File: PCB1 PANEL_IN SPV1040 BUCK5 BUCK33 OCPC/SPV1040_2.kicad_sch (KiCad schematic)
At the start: 14 parts, among them J3 SOLAR, U3 SPV1040TTR

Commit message: w
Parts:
- removed D4: D_Zener, Diode_SMD:D_1210_3225Metric, symbol Device:D_Zener
- added CR3: SMM4F5.0A-TR, CR_F5.0A-TR_STM, symbol SMM4F5:SMM4F5.0A-TR
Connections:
- net GND: now also CR3.1
- net PANEL1_OUT: now also CR3.2
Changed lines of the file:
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@@
-	(wire
-		(pts
-			(xy 104.14 102.87) (xy 106.68 102.87)
-		)
-		(stroke
-			(width 0)
-			(type default)
-		)
-	)
 	(wire
 		(pts
@@
 	)
 	(symbol
+		(lib_id "SMM4F5:SMM4F5.0A-TR")
+		(at 96.52 102.87 0)
+		(unit 1)
+		(exclude_from_sim no)
+		(in_bom yes)
+		(on_board yes)
+		(dnp no)
+		(fields_autoplaced yes)
+		(property "Reference" "CR3"
+			(at 101.6 96.52 0)
+			(effects
+				(font
+					(size 1.524 1.524)
+				)
+			)
+		)
+		(property "Value" "SMM4F5.0A-TR"
+			(at 101.6 99.06 0)
+			(effects
+				(font
+					(size 1.524 1.524)
+				)
+			)
+		)
+		(property "Footprint" "CR_F5.0A-TR_STM"
+			(at 96.52 102.87 0)
+			(effects
+				(font
+					(size 1.27 1.27)
+					(italic yes)
+				)
+				(hide yes)
+			)
+		)
+		(property "Datasheet" "SMM4F5.0A-TR"
+			(at 96.52 102.87 0)
+			(effects
+				(font
+					(size 1.27 1.27)
+					(italic yes)
+				)
+				(hide yes)
+			)
+		)
+		(property "Description" ""
+			(at 96.52 102.87 0)
+			(effects
+				(font
+					(size 1.27 1.27)
+				)
+				(hide yes)
+			)
+		)
+		(pin "1"
+		)
+		(pin "2"
+		)
+		(instances
+			(project "PCB1 PANEL_IN SPV1040 BUCK5 BUCK33 OCPC"
+				(path "/494c9d9f-6b33-4248-a813-27ffaaa929bd/27d3faa1-92c4-4207-bb91-69c494af1bc4"
+					(reference "CR3")
+					(unit 1)
+				)
+			)
+		)
+	)
+	(symbol
 		(lib_id "Device:R")
 		(at 124.46 52.07 0)
@@
 					(unit 1)
 				)
-			)
-		)
-	)
-	(symbol
-		(lib_id "Device:D_Zener")
-		(at 100.33 102.87 180)
-		(unit 1)
-		(exclude_from_sim no)
-		(in_bom yes)
-		(on_board yes)
-		(dnp no)
-		(fields_autoplaced yes)
-		(property "Reference" "D4"
-			(at 100.33 96.52 0)
-			(effects
-				(font
-					(size 1.27 1.27)
-				)
-			)
-		)
-		(property "Value" "D_Zener"
-			(at 100.33 99.06 0)
-			(effects
-				(font
-					(size 1.27 1.27)
-				)
-			)
-		)
-		(property "Footprint" "Diode_SMD:D_1210_3225Metric"
-			(at 100.33 102.87 0)
-			(effects
-				(font
-					(size 1.27 1.27)
-				)
-				(hide yes)
-			)
-		)
-		(property "Datasheet" "~"
-			(at 100.33 102.87 0)
-			(effects
-				(font
-					(size 1.27 1.27)
-				)
-				(hide yes)
-			)
-		)
-		(property "Description" "Zener diode"
-			(at 100.33 102.87 0)
-			(effects
-				(font
-					(size 1.27 1.27)
-				)
-				(hide yes)
-			)
-		)
-		(pin "2"
-		)
-		(pin "1"
-		)
-		(instances
-			(project "PCB1 PANEL_IN SPV1040 BUCK5 BUCK33 OCPC"
-				(path "/494c9d9f-6b33-4248-a813-27ffaaa929bd/27d3faa1-92c4-4207-bb91-69c494af1bc4"
-					(reference "D4")
-					(unit 1)
-				)

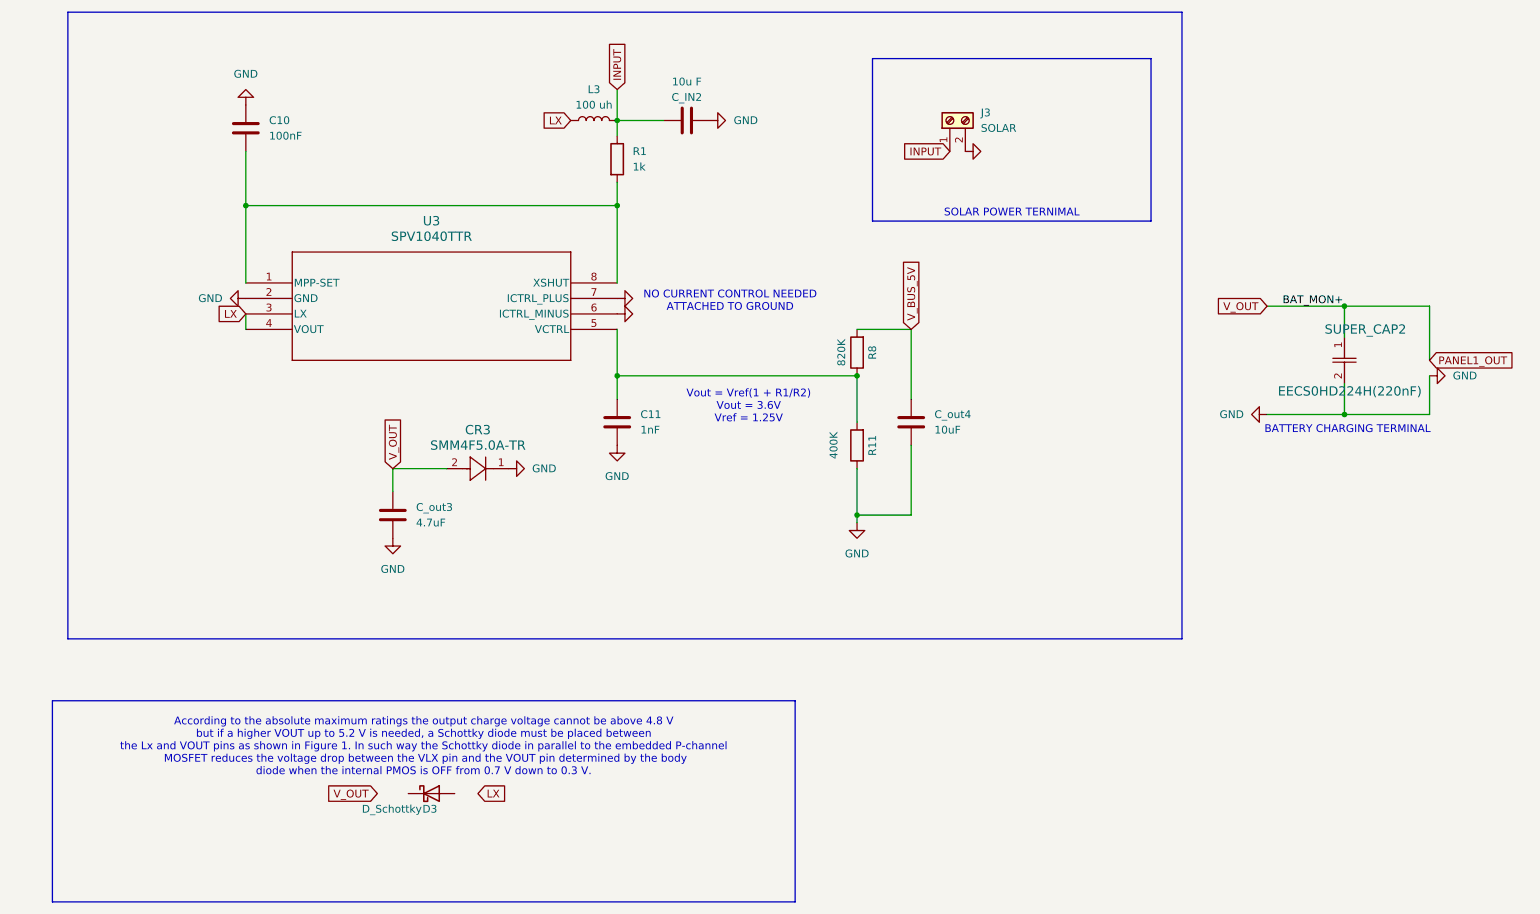
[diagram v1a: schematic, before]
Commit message: Relabeling according to standards
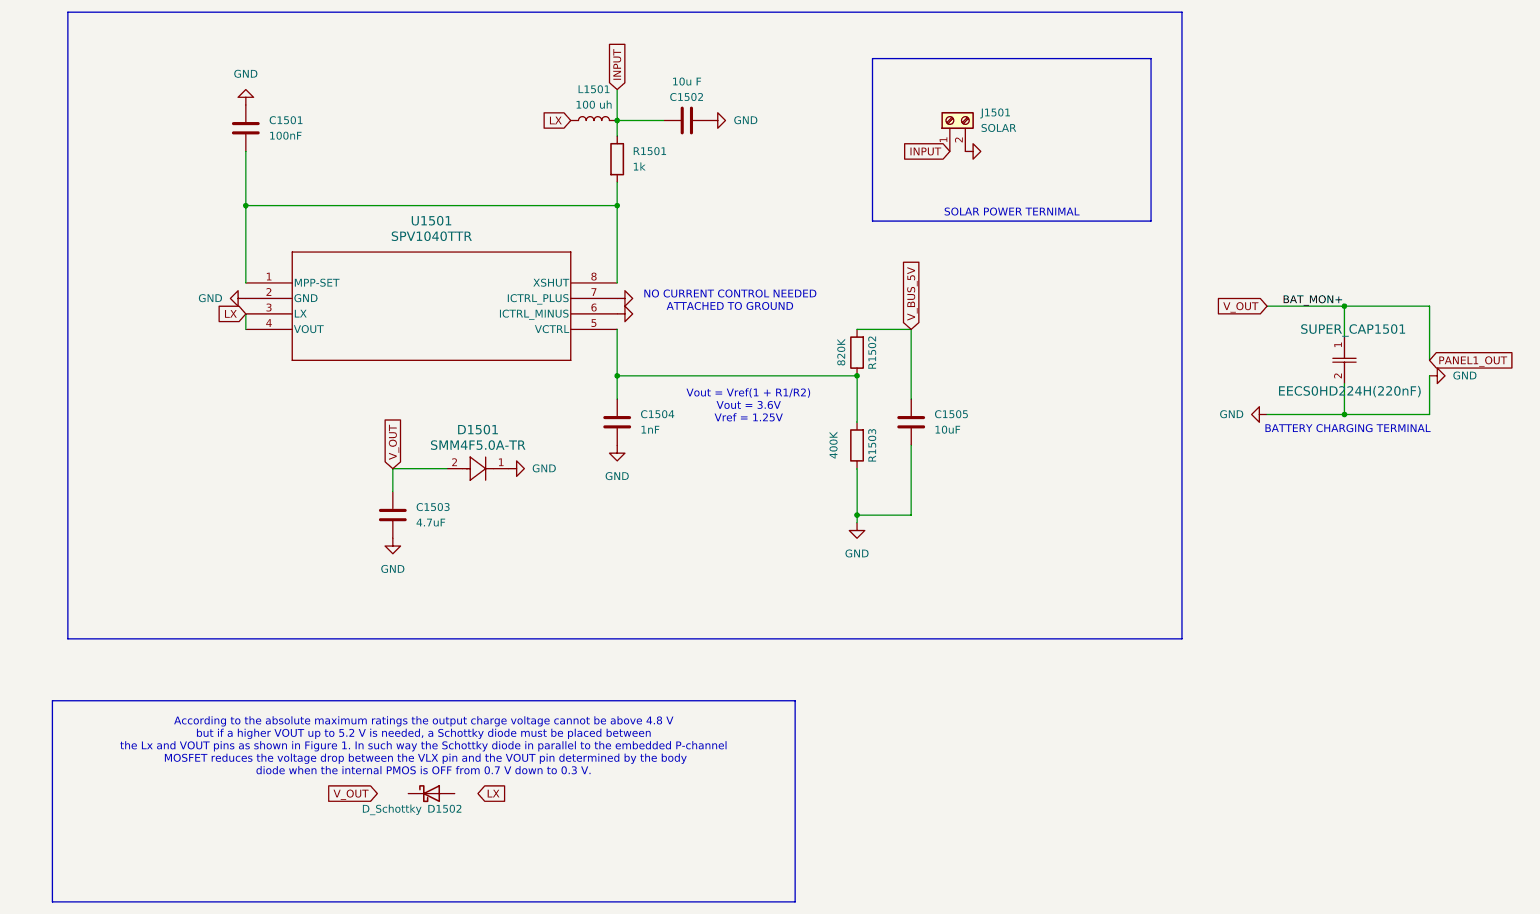
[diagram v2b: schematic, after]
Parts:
- D1501: renamed from CR3; footprint CR_F5.0A-TR_STM -> (none)
- renumbered C10 to C1501, C_IN2 to C1502, C_out3 to C1503, C11 to C1504, C_out4 to C1505, D3 to D1502, J3 to J1501, L3 to L1501, R1 to R1501, R8 to R1502, R11 to R1503, SUPER_CAP2 to SUPER_CAP1501, U3 to U1501
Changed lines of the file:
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@@
 		(dnp no)
 		(fields_autoplaced yes)
-		(property "Reference" "L3"
+		(property "Reference" "L1501"
 			(at 120.65 40.64 90)
 			(effects
@@
 			(project "PCB1 PANEL_IN SPV1040 BUCK5 BUCK33 OCPC"
 				(path "/494c9d9f-6b33-4248-a813-27ffaaa929bd/27d3faa1-92c4-4207-bb91-69c494af1bc4"
-					(reference "L3")
+					(reference "L1501")
 					(unit 1)
 				)
@@
 		(dnp no)
 		(fields_autoplaced yes)
-		(property "Reference" "CR3"
+		(property "Reference" "D1501"
 			(at 101.6 96.52 0)
 			(effects
@@
 			)
 		)
-		(property "Footprint" "CR_F5.0A-TR_STM"
+		(property "Footprint" ""
 			(at 96.52 102.87 0)
 			(effects
@@
 			(project "PCB1 PANEL_IN SPV1040 BUCK5 BUCK33 OCPC"
 				(path "/494c9d9f-6b33-4248-a813-27ffaaa929bd/27d3faa1-92c4-4207-bb91-69c494af1bc4"
-					(reference "CR3")
+					(reference "D1501")
 					(unit 1)
 				)
@@
 		(dnp no)
 		(fields_autoplaced yes)
-		(property "Reference" "R1"
+		(property "Reference" "R1501"
 			(at 127 50.7999 0)
 			(effects
@@
 			(project "PCB1 PANEL_IN SPV1040 BUCK5 BUCK33 OCPC"
 				(path "/494c9d9f-6b33-4248-a813-27ffaaa929bd/27d3faa1-92c4-4207-bb91-69c494af1bc4"
-					(reference "R1")
+					(reference "R1501")
 					(unit 1)
 				)
@@
 		(dnp no)
 		(fields_autoplaced yes)
-		(property "Reference" "C11"
+		(property "Reference" "C1504"
 			(at 128.27 93.9799 0)
 			(effects
@@
 			(project "PCB1 PANEL_IN SPV1040 BUCK5 BUCK33 OCPC"
 				(path "/494c9d9f-6b33-4248-a813-27ffaaa929bd/27d3faa1-92c4-4207-bb91-69c494af1bc4"
-					(reference "C11")
+					(reference "C1504")
 					(unit 1)
 				)
@@
 		(dnp no)
 		(fields_autoplaced yes)
-		(property "Reference" "C_out4"
+		(property "Reference" "C1505"
 			(at 176.53 93.9799 0)
 			(effects
@@
 			(project "PCB1 PANEL_IN SPV1040 BUCK5 BUCK33 OCPC"
 				(path "/494c9d9f-6b33-4248-a813-27ffaaa929bd/27d3faa1-92c4-4207-bb91-69c494af1bc4"
-					(reference "C_out4")
+					(reference "C1505")
 					(unit 1)
 				)
@@
 		(on_board yes)
 		(dnp no)
-		(property "Reference" "SUPER_CAP2"
+		(property "Reference" "SUPER_CAP1501"
 			(at 254 80.01 90)
 			(effects
@@
 			(project "PCB1 PANEL_IN SPV1040 BUCK5 BUCK33 OCPC"
 				(path "/494c9d9f-6b33-4248-a813-27ffaaa929bd/27d3faa1-92c4-4207-bb91-69c494af1bc4"
-					(reference "SUPER_CAP2")
+					(reference "SUPER_CAP1501")
 					(unit 1)
 				)
@@
 		(on_board yes)
 		(dnp no)
-		(property "Reference" "R11"
+		(property "Reference" "R1503"
 			(at 166.37 99.06 90)
 			(effects
@@
 			(project "PCB1 PANEL_IN SPV1040 BUCK5 BUCK33 OCPC"
 				(path "/494c9d9f-6b33-4248-a813-27ffaaa929bd/27d3faa1-92c4-4207-bb91-69c494af1bc4"
-					(reference "R11")
+					(reference "R1503")
 					(unit 1)
 				)
@@
 		(dnp no)
 		(fields_autoplaced yes)
-		(property "Reference" "C10"
+		(property "Reference" "C1501"
 			(at 67.31 45.7199 0)
 			(effects
@@
 			(project "PCB1 PANEL_IN SPV1040 BUCK5 BUCK33 OCPC"
 				(path "/494c9d9f-6b33-4248-a813-27ffaaa929bd/27d3faa1-92c4-4207-bb91-69c494af1bc4"
-					(reference "C10")
+					(reference "C1501")
 					(unit 1)
 				)
@@
 		(dnp no)
 		(fields_autoplaced yes)
-		(property "Reference" "U3"
+		(property "Reference" "U1501"
 			(at 93.98 62.23 0)
 			(effects
@@
 			(project "PCB1 PANEL_IN SPV1040 BUCK5 BUCK33 OCPC"
 				(path "/494c9d9f-6b33-4248-a813-27ffaaa929bd/27d3faa1-92c4-4207-bb91-69c494af1bc4"
-					(reference "U3")
+					(reference "U1501")
 					(unit 1)
 				)
@@
 		(on_board yes)
 		(dnp no)
-		(property "Reference" "C_IN2"
+		(property "Reference" "C1502"
 			(at 135.89 41.91 90)
 			(effects
@@
 			(project "PCB1 PANEL_IN SPV1040 BUCK5 BUCK33 OCPC"
 				(path "/494c9d9f-6b33-4248-a813-27ffaaa929bd/27d3faa1-92c4-4207-bb91-69c494af1bc4"
-					(reference "C_IN2")
+					(reference "C1502")
 					(unit 1)
 				)
@@
 		(on_board yes)
 		(dnp no)
-		(property "Reference" "R8"
+		(property "Reference" "R1502"
 			(at 166.37 83.82 90)
 			(effects
@@
 			(project "PCB1 PANEL_IN SPV1040 BUCK5 BUCK33 OCPC"
 				(path "/494c9d9f-6b33-4248-a813-27ffaaa929bd/27d3faa1-92c4-4207-bb91-69c494af1bc4"
-					(reference "R8")
+					(reference "R1502")
 					(unit 1)
 				)
@@
 		(dnp no)
 		(fields_autoplaced yes)
-		(property "Reference" "J3"
+		(property "Reference" "J1501"
 			(at 184.15 44.4499 90)
 			(effects
@@
 			(project "PCB1 PANEL_IN SPV1040 BUCK5 BUCK33 OCPC"
 				(path "/494c9d9f-6b33-4248-a813-27ffaaa929bd/27d3faa1-92c4-4207-bb91-69c494af1bc4"
-					(reference "J3")
+					(reference "J1501")
 					(unit 1)
 				)
@@
 		(dnp no)
 		(fields_autoplaced yes)
-		(property "Reference" "C_out3"
+		(property "Reference" "C1503"
 			(at 91.44 109.2199 0)
 			(effects
@@
 			(project "PCB1 PANEL_IN SPV1040 BUCK5 BUCK33 OCPC"
 				(path "/494c9d9f-6b33-4248-a813-27ffaaa929bd/27d3faa1-92c4-4207-bb91-69c494af1bc4"
-					(reference "C_out3")
+					(reference "C1503")
 					(unit 1)
 				)
@@
 		(on_board yes)
 		(dnp no)
-		(property "Reference" "D3"
-			(at 94.9326 158.75 0)
+		(property "Reference" "D1502"
+			(at 99.06 158.75 0)
 			(effects
 				(font
@@
 			(project "PCB1 PANEL_IN SPV1040 BUCK5 BUCK33 OCPC"
 				(path "/494c9d9f-6b33-4248-a813-27ffaaa929bd/27d3faa1-92c4-4207-bb91-69c494af1bc4"
-					(reference "D3")
-					(unit 1)
-				)
+					(reference "D1502")
+					(unit 1)
+				)
